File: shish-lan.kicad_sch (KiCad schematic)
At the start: 7 parts

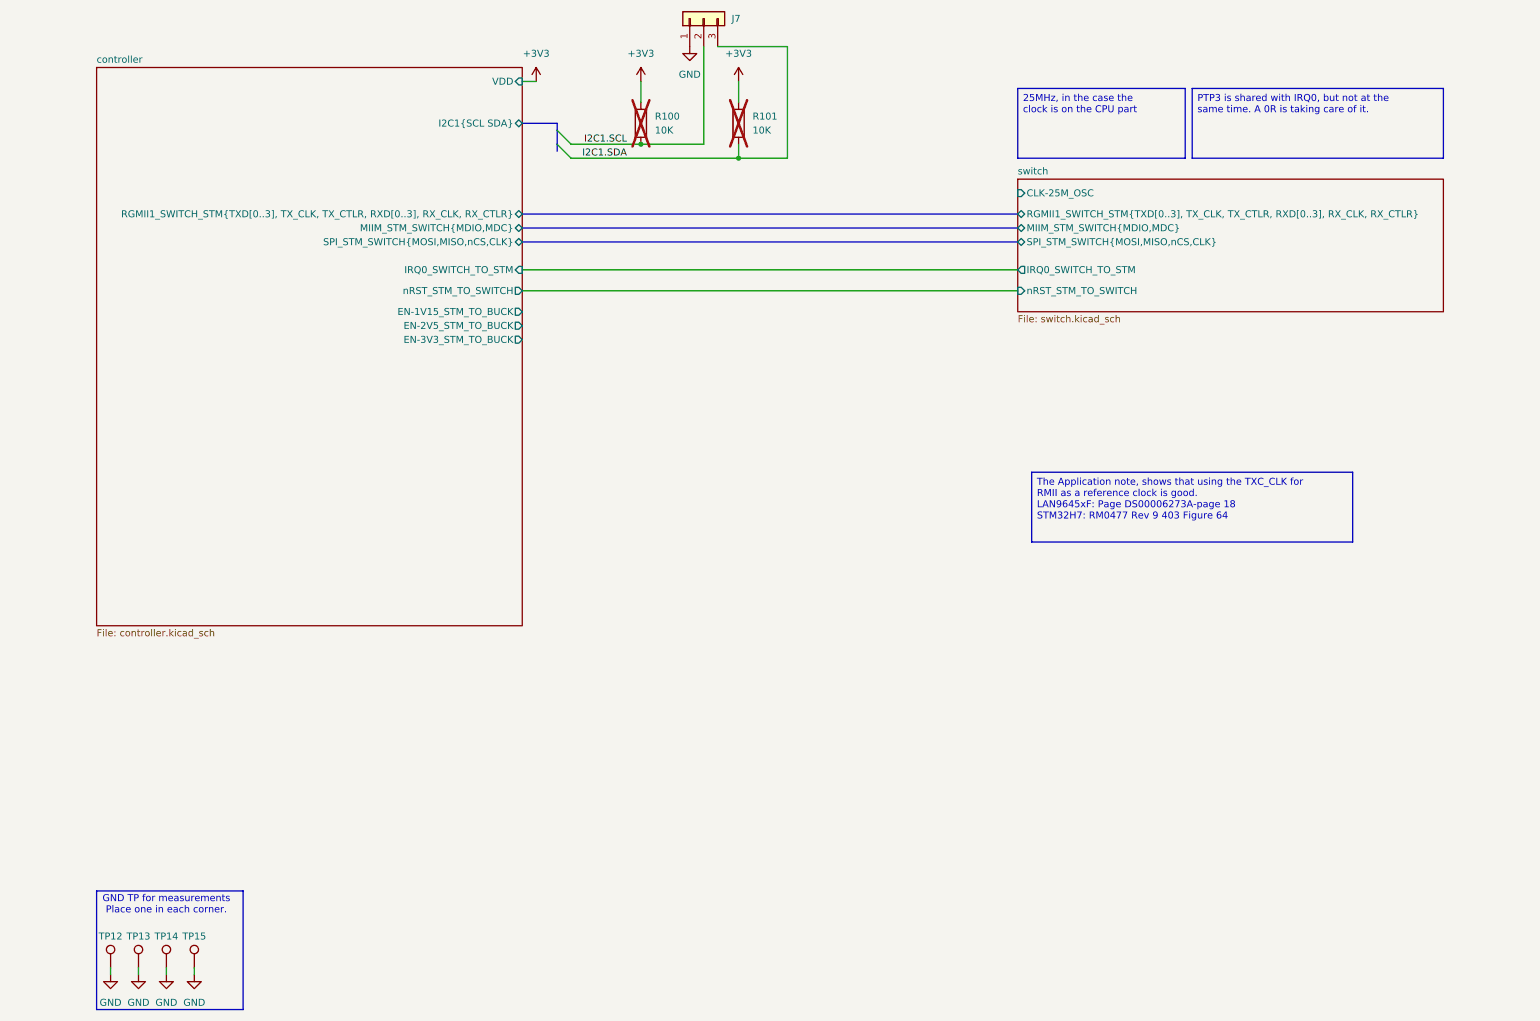
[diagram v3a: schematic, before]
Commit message: moves +3V3 converter to root. Refs: #1
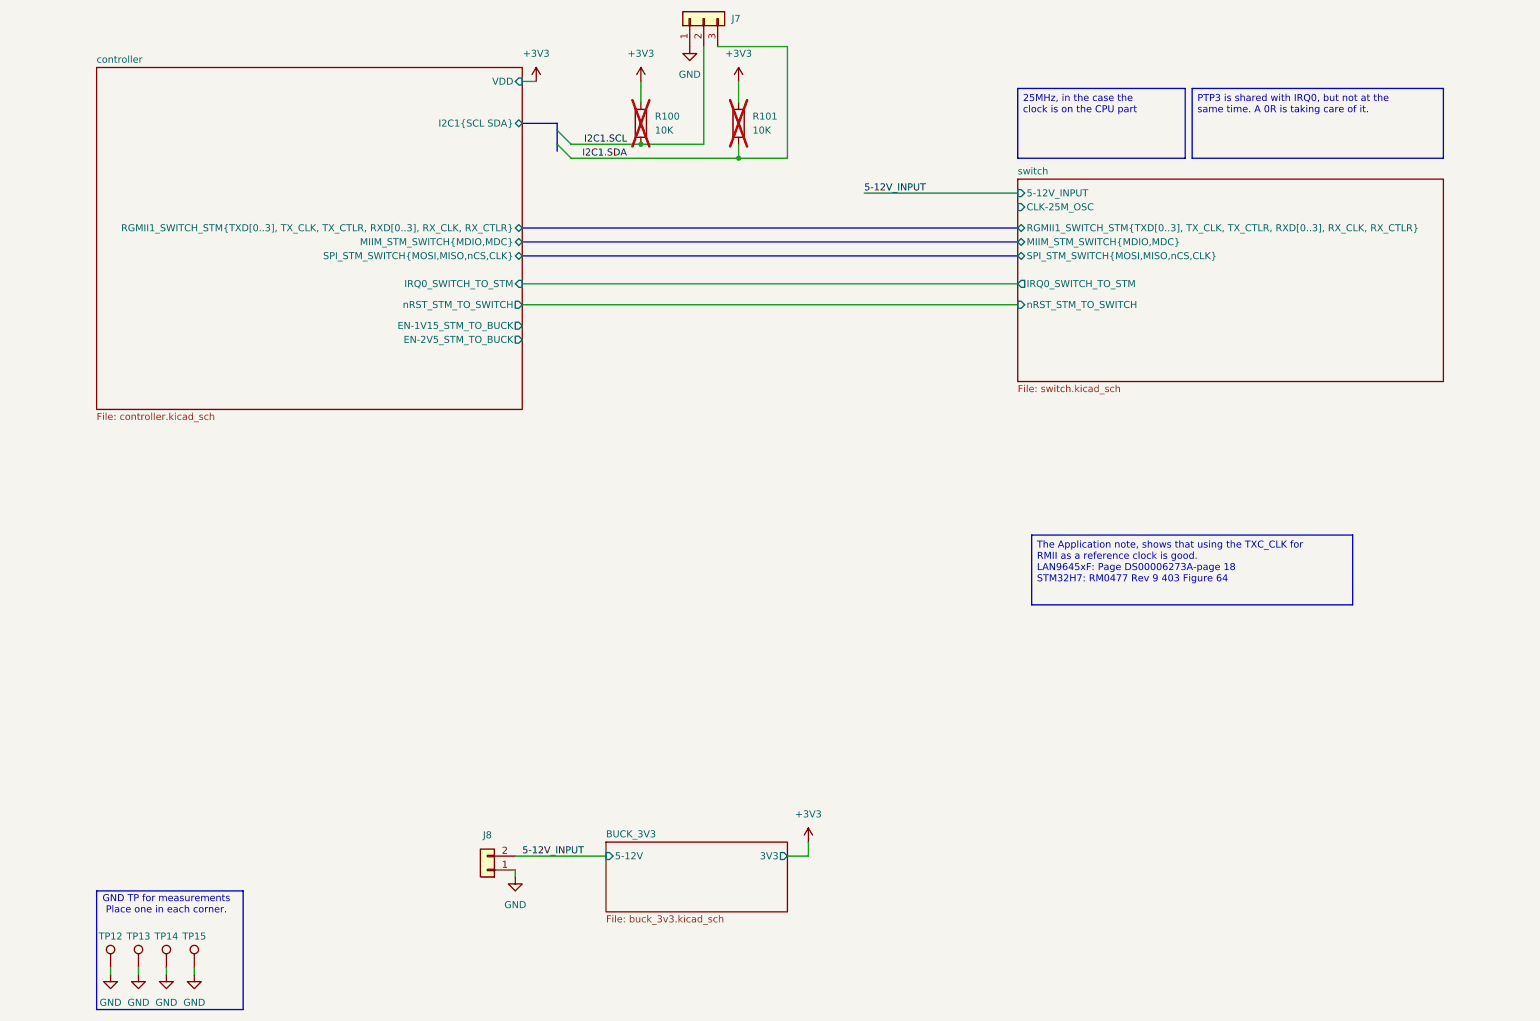
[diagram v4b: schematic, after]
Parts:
- added J8: ~, KL:02x01_2.54mm_Header, symbol KL_Headers:02x01_2.54mm_Header
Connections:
- net GND: now also J8.1 (Pin_1)
- new net 5-12V_INPUT: J8.2 (Pin_2)
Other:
- added sheet BUCK_3V3 (buck_3v3.kicad_sch)
- sheet controller ports: added none; removed EN-3V3_STM_TO_BUCK
- sheet switch ports: added 5-12V_INPUT; removed none

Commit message: connects 1V15 and 2V5 to STM. Refs: #1
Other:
- sheet switch ports: added EN-1V15_STM_TO_BUCK, EN-2V5_STM_TO_BUCK; removed none
- moved on the sheet: J8
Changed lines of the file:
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@@
 	(wire
 		(pts
-			(xy 143.51 167.64) (xy 147.32 167.64)
+			(xy 132.08 127) (xy 135.89 127)
 		)
 		(stroke
@@
 	(wire
 		(pts
-			(xy 93.98 171.45) (xy 93.98 170.18)
+			(xy 82.55 130.81) (xy 82.55 129.54)
 		)
 		(stroke
@@
 	(wire
 		(pts
-			(xy 93.98 167.64) (xy 110.49 167.64)
+			(xy 82.55 127) (xy 99.06 127)
 		)
 		(stroke
@@
 	(wire
 		(pts
-			(xy 147.32 165.1) (xy 147.32 167.64)
+			(xy 95.25 73.66) (xy 185.42 73.66)
+		)
+		(stroke
+			(width 0)
+			(type default)
+		)
+	)
+	(wire
+		(pts
+			(xy 135.89 124.46) (xy 135.89 127)
 		)
 		(stroke
@@
 	(wire
 		(pts
+			(xy 95.25 71.12) (xy 185.42 71.12)
+		)
+		(stroke
+			(width 0)
+			(type default)
+		)
+	)
+	(wire
+		(pts
 			(xy 128.27 20.32) (xy 128.27 38.1)
 		)
@@
 	)
 	(label "5-12V_INPUT"
-		(at 95.25 167.64 0)
+		(at 83.82 127 0)
 		(effects
 			(font
@@
 	(symbol
 		(lib_id "power:+3V3")
-		(at 147.32 165.1 0)
+		(at 135.89 124.46 0)
 		(unit 1)
 		(exclude_from_sim no)
@@
 		(fields_autoplaced yes)
 		(property "Reference" "#PWR01"
-			(at 147.32 168.91 0)
+			(at 135.89 128.27 0)
 			(effects
 				(font
@@
 		)
 		(property "Value" "+3V3"
-			(at 147.32 160.02 0)
+			(at 135.89 119.38 0)
 			(effects
 				(font
@@
 		)
 		(property "Footprint" ""
-			(at 147.32 165.1 0)
+			(at 135.89 124.46 0)
 			(effects
 				(font
@@
 		)
 		(property "Datasheet" ""
-			(at 147.32 165.1 0)
+			(at 135.89 124.46 0)
 			(effects
 				(font
@@
 		)
 		(property "Description" "Power symbol creates a global label with name \"+3V3\""
-			(at 147.32 165.1 0)
+			(at 135.89 124.46 0)
 			(effects
 				(font
@@
 	(symbol
 		(lib_id "KL_Headers:02x01_2.54mm_Header")
-		(at 88.9 168.91 180)
+		(at 77.47 128.27 180)
 		(unit 1)
 		(exclude_from_sim no)
@@
 		(fields_autoplaced yes)
 		(property "Reference" "J8"
-			(at 88.9 163.83 0)
+			(at 77.47 123.19 0)
 			(effects
 				(font
@@
 		)
 		(property "Value" "~"
-			(at 88.9 168.91 0)
+			(at 77.47 128.27 0)
 			(effects
 				(font
@@
 		)
 		(property "Footprint" "KL:02x01_2.54mm_Header"
-			(at 88.9 168.91 0)
+			(at 77.47 128.27 0)
 			(effects
 				(font
@@
 		)
 		(property "Datasheet" ""
-			(at 88.9 168.91 0)
+			(at 77.47 128.27 0)
 			(effects
 				(font
@@
 		)
 		(property "Description" ""
-			(at 88.9 168.91 0)
+			(at 77.47 128.27 0)
 			(effects
 				(font
@@
 	(symbol
 		(lib_id "KL_SYM_LOCAL:GND")
-		(at 93.98 171.45 0)
+		(at 82.55 130.81 0)
 		(unit 1)
 		(exclude_from_sim no)
@@
 		(fields_autoplaced yes)
 		(property "Reference" "#PWR02"
-			(at 93.98 177.8 0)
+			(at 82.55 137.16 0)
 			(effects
 				(font
@@
 		)
 		(property "Value" "GND"
-			(at 93.98 176.53 0)
+			(at 82.55 135.89 0)
 			(effects
 				(font
@@
 		)
 		(property "Footprint" ""
-			(at 93.98 171.45 0)
+			(at 82.55 130.81 0)
 			(effects
 				(font
@@
 		)
 		(property "Datasheet" ""
-			(at 93.98 171.45 0)
+			(at 82.55 130.81 0)
 			(effects
 				(font
@@
 		)
 		(property "Description" "Power symbol creates a global label with name \"GND\" , ground"
-			(at 93.98 171.45 0)
+			(at 82.55 130.81 0)
 			(effects
 				(font
@@
 			)
 		)
+		(pin "EN-1V15_STM_TO_BUCK" input
+			(at 185.42 71.12 180)
+			(effects
+				(font
+					(size 1.27 1.27)
+				)
+				(justify left)
+			)
+		)
+		(pin "EN-2V5_STM_TO_BUCK" input
+			(at 185.42 73.66 180)
+			(effects
+				(font
+					(size 1.27 1.27)
+				)
+				(justify left)
+			)
+		)
 		(instances
 			(project "shish-lan"
@@
 	)
 	(sheet
-		(at 110.49 165.1)
+		(at 99.06 124.46)
 		(size 33.02 12.7)
 		(exclude_from_sim no)
@@
 		)
 		(property "Sheetname" "BUCK_3V3"
-			(at 110.49 164.3884 0)
+			(at 99.06 123.7484 0)
 			(effects
 				(font
@@
 		)
 		(property "Sheetfile" "buck_3v3.kicad_sch"
-			(at 110.49 178.3846 0)
+			(at 99.06 137.7446 0)
 			(effects
 				(font
@@
 		)
 		(pin "3V3" output
-			(at 143.51 167.64 0)
+			(at 132.08 127 0)
 			(effects
 				(font
@@
 		)
 		(pin "5-12V" input
-			(at 110.49 167.64 180)
+			(at 99.06 127 180)
 			(effects
 				(font

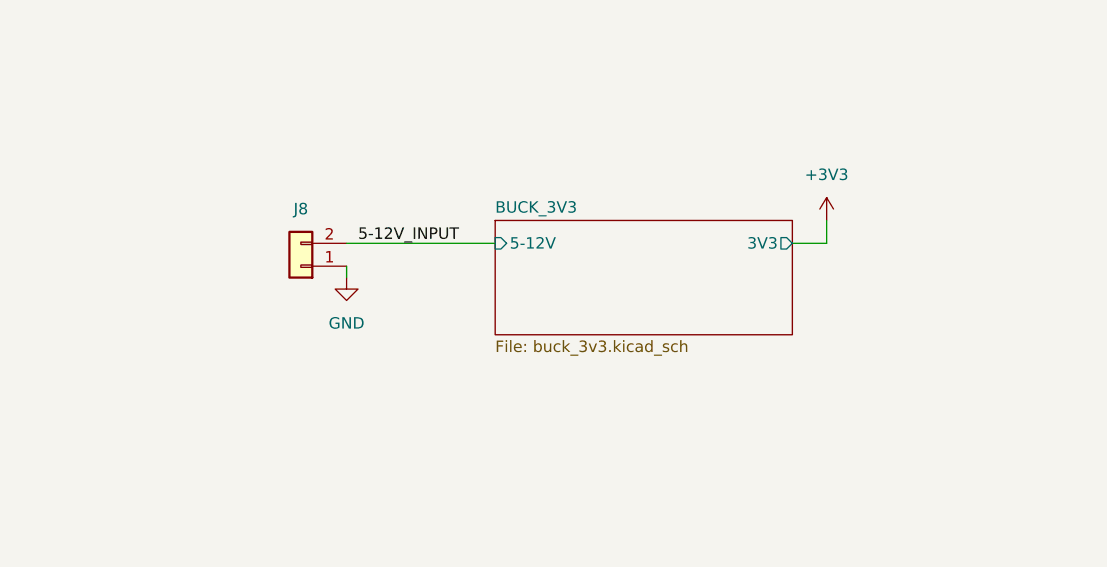
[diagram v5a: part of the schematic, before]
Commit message: fixes ERC errors in DC/DC converters
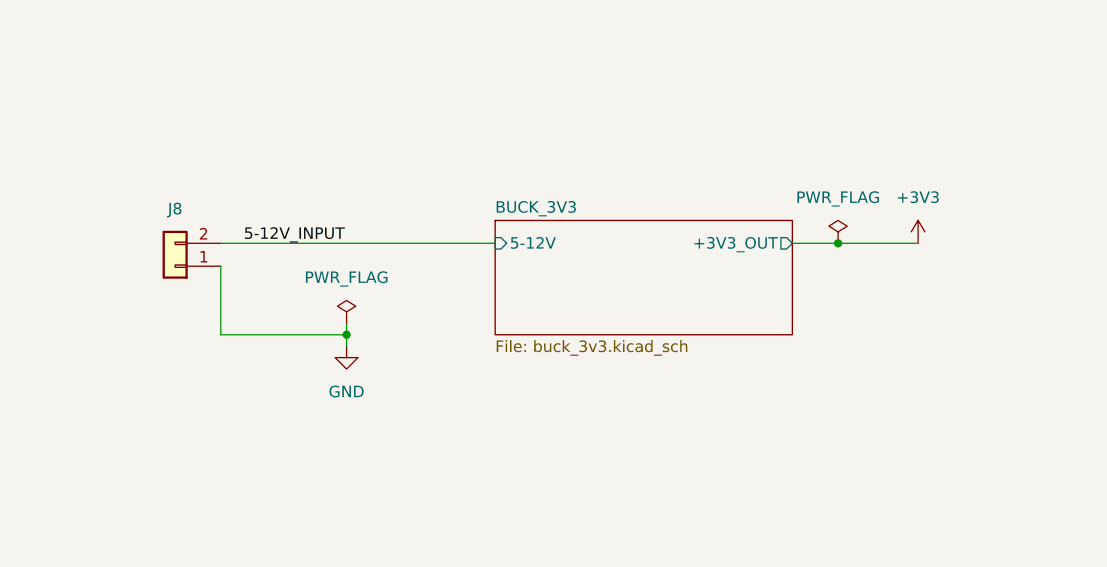
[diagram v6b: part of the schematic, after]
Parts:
- J8: footprint KL:02x01_2.54mm_Header -> KL_Footprints:02x01_2.54mm_Header
- R100, R101: footprint KL_Footprints:C_0603 -> KL_Footprints:R_0603; now in the parts list
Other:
- sheet BUCK_3V3 ports: added +3V3_OUT; removed 3V3
- moved on the sheet: J8
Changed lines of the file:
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@@
 	)
 	(junction
+		(at 137.16 127)
+		(diameter 0)
+		(color 0 0 0 0)
+	)
+	(junction
 		(at 116.84 38.1)
 		(diameter 0)
 		(color 0 0 0 0)
 	)
+	(junction
+		(at 82.55 137.16)
+		(diameter 0)
+		(color 0 0 0 0)
+	)
 	(bus_entry
 		(at 101.6 35.56)
@@
 	(wire
 		(pts
-			(xy 132.08 127) (xy 135.89 127)
+			(xy 132.08 127) (xy 137.16 127)
 		)
 		(stroke
@@
 	(wire
 		(pts
-			(xy 20.32 189.23) (xy 20.32 187.96)
+			(xy 82.55 135.89) (xy 82.55 137.16)
 		)
 		(stroke
@@
 	(wire
 		(pts
-			(xy 35.56 189.23) (xy 35.56 187.96)
+			(xy 20.32 189.23) (xy 20.32 187.96)
 		)
 		(stroke
@@
 	(wire
 		(pts
-			(xy 82.55 130.81) (xy 82.55 129.54)
+			(xy 35.56 189.23) (xy 35.56 187.96)
 		)
 		(stroke
@@
 	(wire
 		(pts
-			(xy 82.55 127) (xy 99.06 127)
+			(xy 68.58 127) (xy 99.06 127)
+		)
+		(stroke
+			(width 0)
+			(type default)
+		)
+	)
+	(wire
+		(pts
+			(xy 82.55 138.43) (xy 82.55 137.16)
 		)
 		(stroke
@@
 	(wire
 		(pts
-			(xy 135.89 124.46) (xy 135.89 127)
+			(xy 137.16 127) (xy 146.05 127)
+		)
+		(stroke
+			(width 0)
+			(type default)
+		)
+	)
+	(wire
+		(pts
+			(xy 82.55 137.16) (xy 68.58 137.16)
 		)
 		(stroke
@@
 	(wire
 		(pts
+			(xy 68.58 137.16) (xy 68.58 129.54)
+		)
+		(stroke
+			(width 0)
+			(type default)
+		)
+	)
+	(wire
+		(pts
 			(xy 157.48 46.99) (xy 185.42 46.99)
 		)
@@
 	)
 	(label "5-12V_INPUT"
-		(at 83.82 127 0)
+		(at 71.12 127 0)
 		(effects
 			(font
@@
 	(symbol
 		(lib_id "power:+3V3")
-		(at 135.89 124.46 0)
+		(at 146.05 127 0)
 		(unit 1)
 		(exclude_from_sim no)
@@
 		(fields_autoplaced yes)
 		(property "Reference" "#PWR01"
-			(at 135.89 128.27 0)
+			(at 146.05 130.81 0)
 			(effects
 				(font
@@
 		)
 		(property "Value" "+3V3"
-			(at 135.89 119.38 0)
+			(at 146.05 121.92 0)
 			(effects
 				(font
@@
 		)
 		(property "Footprint" ""
-			(at 135.89 124.46 0)
+			(at 146.05 127 0)
 			(effects
 				(font
@@
 		)
 		(property "Datasheet" ""
-			(at 135.89 124.46 0)
+			(at 146.05 127 0)
 			(effects
 				(font
@@
 		)
 		(property "Description" "Power symbol creates a global label with name \"+3V3\""
-			(at 135.89 124.46 0)
+			(at 146.05 127 0)
 			(effects
 				(font
@@
 		(unit 1)
 		(exclude_from_sim no)
-		(in_bom no)
+		(in_bom yes)
 		(on_board yes)
 		(dnp yes)
@@
 			)
 		)
-		(property "Footprint" "KL_Footprints:C_0603"
+		(property "Footprint" "KL_Footprints:R_0603"
 			(at 132.842 34.29 90)
 			(effects
@@
 	(symbol
 		(lib_id "KL_Headers:02x01_2.54mm_Header")
-		(at 77.47 128.27 180)
+		(at 63.5 128.27 180)
 		(unit 1)
 		(exclude_from_sim no)
@@
 		(fields_autoplaced yes)
 		(property "Reference" "J8"
-			(at 77.47 123.19 0)
+			(at 63.5 123.19 0)
 			(effects
 				(font
@@
 		)
 		(property "Value" "~"
-			(at 77.47 128.27 0)
+			(at 63.5 128.27 0)
 			(effects
 				(font
@@
 			)
 		)
-		(property "Footprint" "KL:02x01_2.54mm_Header"
-			(at 77.47 128.27 0)
+		(property "Footprint" "KL_Footprints:02x01_2.54mm_Header"
+			(at 63.5 128.27 0)
 			(effects
 				(font
@@
 		)
 		(property "Datasheet" ""
-			(at 77.47 128.27 0)
+			(at 63.5 128.27 0)
 			(effects
 				(font
@@
 		)
 		(property "Description" ""
-			(at 77.47 128.27 0)
+			(at 63.5 128.27 0)
 			(effects
 				(font
@@
 		(unit 1)
 		(exclude_from_sim no)
-		(in_bom no)
+		(in_bom yes)
 		(on_board yes)
 		(dnp yes)
@@
 			)
 		)
-		(property "Footprint" "KL_Footprints:C_0603"
+		(property "Footprint" "KL_Footprints:R_0603"
 			(at 115.062 34.29 90)
 			(effects
@@
 	)
 	(symbol
+		(lib_id "KL_Flags:PWR_FLAG")
+		(at 137.16 127 0)
+		(unit 1)
+		(exclude_from_sim no)
+		(in_bom yes)
+		(on_board yes)
+		(dnp no)
+		(fields_autoplaced yes)
+		(property "Reference" "#FLG02"
+			(at 137.16 125.095 0)
+			(effects
+				(font
+					(size 1.27 1.27)
+				)
+				(hide yes)
+			)
+		)
+		(property "Value" "PWR_FLAG"
+			(at 137.16 121.92 0)
+			(effects
+				(font
+					(size 1.27 1.27)
+				)
+			)
+		)
+		(property "Footprint" ""
+			(at 137.16 127 0)
+			(effects
+				(font
+					(size 1.27 1.27)
+				)
+				(hide yes)
+			)
+		)
+		(property "Datasheet" "~"
+			(at 137.16 127 0)
+			(effects
+				(font
+					(size 1.27 1.27)
+				)
+				(hide yes)
+			)
+		)
+		(property "Description" "Special symbol for telling ERC where power comes from"
+			(at 137.16 127 0)
+			(effects
+				(font
+					(size 1.27 1.27)
+				)
+				(hide yes)
+			)
+		)
+		(pin "1"
+		)
+		(instances
+			(project ""
+				(path "/d4536448-b109-4159-96e2-3dc21baf2d6e"
+					(reference "#FLG02")
+					(unit 1)
+				)
+			)
+		)
+	)
+	(symbol
+		(lib_id "KL_Flags:PWR_FLAG")
+		(at 82.55 135.89 0)
+		(unit 1)
+		(exclude_from_sim no)
+		(in_bom yes)
+		(on_board yes)
+		(dnp no)
+		(fields_autoplaced yes)
+		(property "Reference" "#FLG1"
+			(at 82.55 133.985 0)
+			(effects
+				(font
+					(size 1.27 1.27)
+				)
+				(hide yes)
+			)
+		)
+		(property "Value" "PWR_FLAG"
+			(at 82.55 130.81 0)
+			(effects
+				(font
+					(size 1.27 1.27)
+				)
+			)
+		)
+		(property "Footprint" ""
+			(at 82.55 135.89 0)
+			(effects
+				(font
+					(size 1.27 1.27)
+				)
+				(hide yes)
+			)
+		)
+		(property "Datasheet" "~"
+			(at 82.55 135.89 0)
+			(effects
+				(font
+					(size 1.27 1.27)
+				)
+				(hide yes)
+			)
+		)
+		(property "Description" "Special symbol for telling ERC where power comes from"
+			(at 82.55 135.89 0)
+			(effects
+				(font
+					(size 1.27 1.27)
+				)
+				(hide yes)
+			)
+		)
+		(pin "1"
+		)
+		(instances
+			(project ""
+				(path "/d4536448-b109-4159-96e2-3dc21baf2d6e"
+					(reference "#FLG1")
+					(unit 1)
+				)
+			)
+		)
+	)
+	(symbol
 		(lib_id "KL_SYM_LOCAL:GND")
 		(at 125.73 20.32 0)
@@
 	(symbol
 		(lib_id "KL_SYM_LOCAL:GND")
-		(at 82.55 130.81 0)
+		(at 82.55 138.43 0)
 		(unit 1)
 		(exclude_from_sim no)
@@
 		(fields_autoplaced yes)
 		(property "Reference" "#PWR02"
-			(at 82.55 137.16 0)
+			(at 82.55 144.78 0)
 			(effects
 				(font
@@
 		)
 		(property "Value" "GND"
-			(at 82.55 135.89 0)
+			(at 82.55 143.51 0)
 			(effects
 				(font
@@
 		)
 		(property "Footprint" ""
-			(at 82.55 130.81 0)
+			(at 82.55 138.43 0)
 			(effects
 				(font
@@
 		)
 		(property "Datasheet" ""
-			(at 82.55 130.81 0)
+			(at 82.55 138.43 0)
 			(effects
 				(font
@@
 		)
 		(property "Description" "Power symbol creates a global label with name \"GND\" , ground"
-			(at 82.55 130.81 0)
+			(at 82.55 138.43 0)
 			(effects
 				(font
@@
 			)
 		)
-		(pin "3V3" output
+		(pin "+3V3_OUT" output
 			(at 132.08 127 0)
 			(effects

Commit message: updates pin headers
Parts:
- J7: footprint KL:03x01_2.54mm_Header -> KL_Footprints:03x01_2.54mm_Header
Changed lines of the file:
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@@
 			)
 		)
-		(property "Footprint" "KL:03x01_2.54mm_Header"
+		(property "Footprint" "KL_Footprints:03x01_2.54mm_Header"
 			(at 119.888 14.478 0)
 			(effects
